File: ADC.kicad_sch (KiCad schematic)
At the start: 20 parts, among them U6 TLV320ADC5140IRTWR, U7 TLV320ADC5140IRTWR

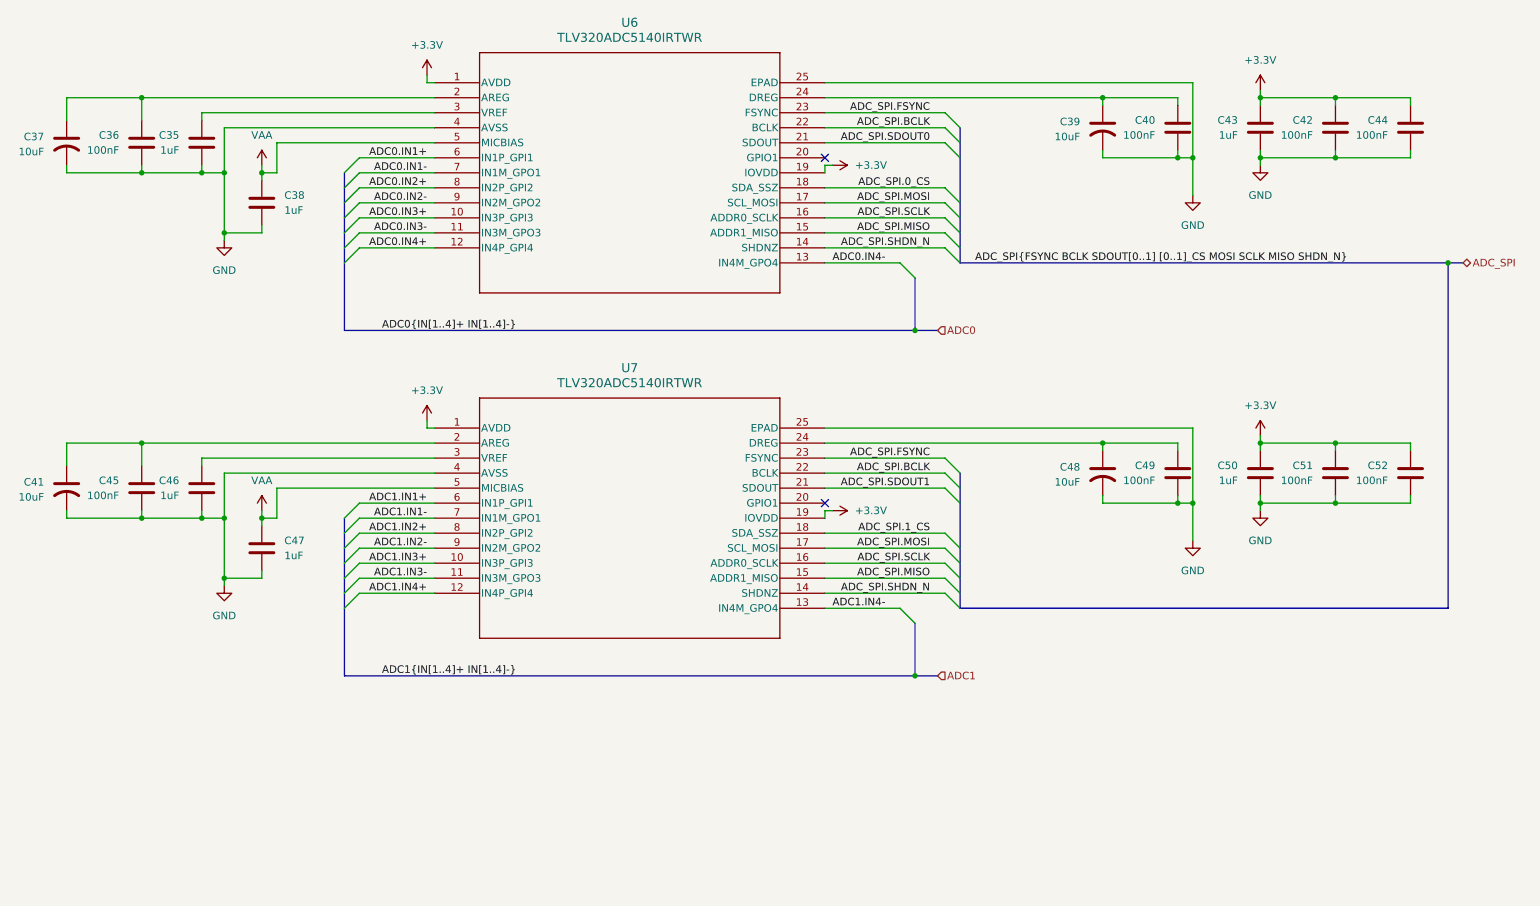
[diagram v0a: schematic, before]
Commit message: Added SRAM and removed old ADC
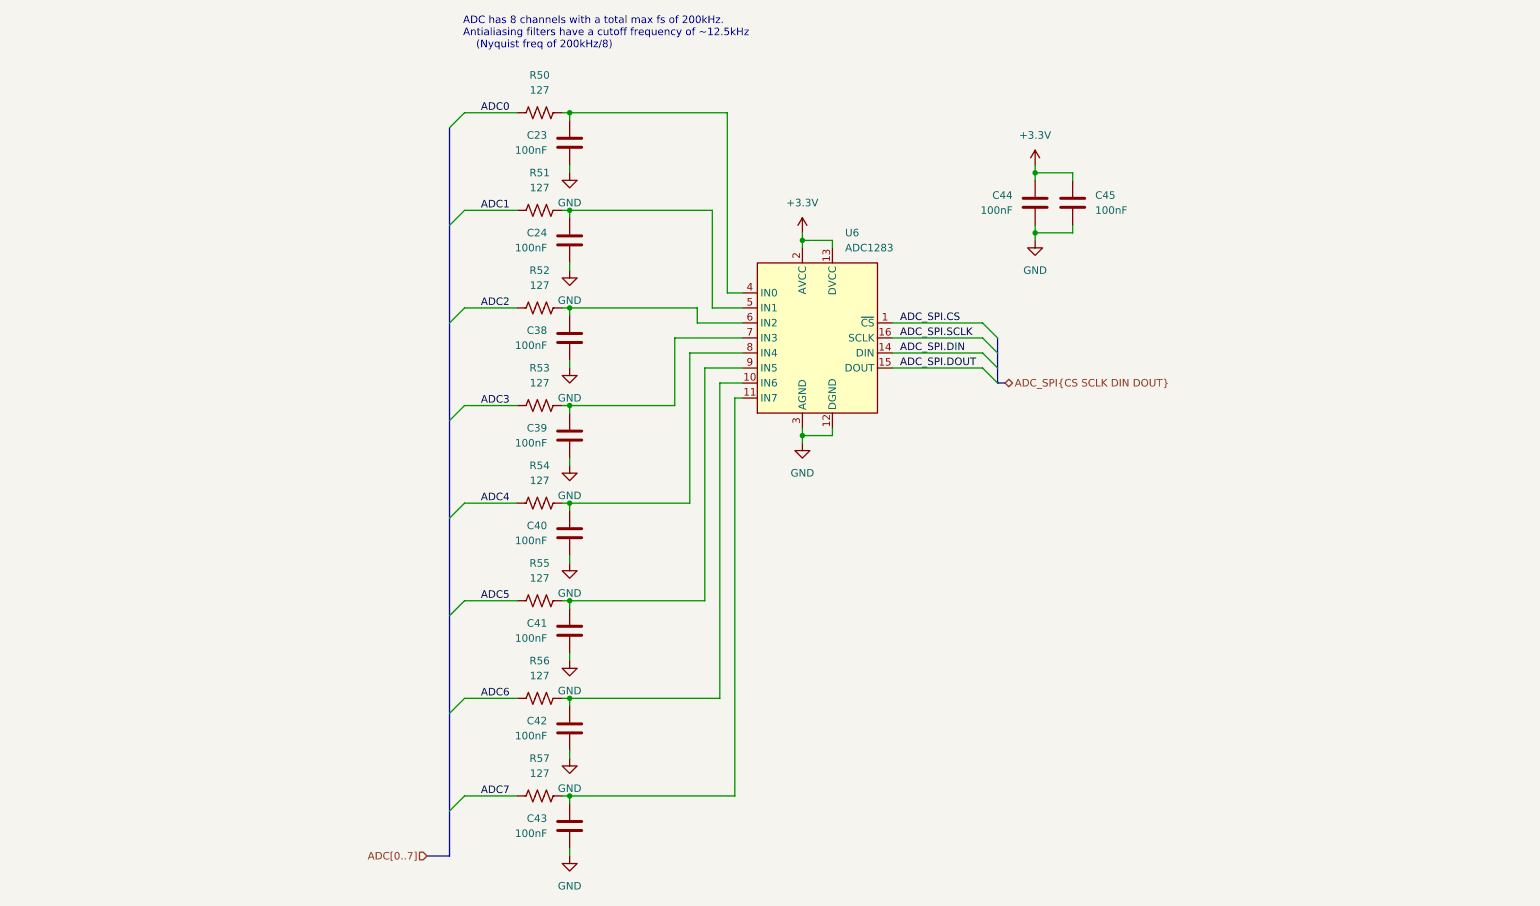
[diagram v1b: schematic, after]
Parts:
- removed C35, C46, C47, C50: 1uF, Capacitor_SMD:C_0603_1608Metric, symbol Device:C
- removed C36, C49, C51, C52: 100nF, Capacitor_SMD:C_0603_1608Metric, symbol Device:C
- removed C37, C39, C41, C48: 10uF, symbol Device:C_US
- removed U6, U7: TLV320ADC5140IRTWR, TLV320ADC5140:RTW24_4P15X4P15_TEX, symbol TLV320ADC5140:TLV320ADC5140IRTWR
- added C23, C24, C39, C41: 100nF, Capacitor_SMD:C_0603_1608Metric, symbol Device:C
- added R50, R51, R52, R53, R54, R55, R56, R57: 127, Resistor_SMD:R_0603_1608Metric, symbol Device:R_US
- added U6: ADC1283, Package_SO:TSSOP-16_4.4x5mm_P0.65mm, symbol Analog_ADC:ADC1283
- C38, C43: value 1uF -> 100nF
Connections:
- net +3.3V: now also C45.1, U6.13 (DVCC), U6.2 (AVCC); no longer C42.1, C43.1
- net ADC0: now also R50.1
- net ADC1: now also R51.1
- net ADC_SPI.SCLK: now also U6.16 (SCLK)
- net GND: now also C23.2, C24.2, C39.2, C41.2, U6.12 (DGND), U6.3 (AGND)
- net at C40.1: now also R54.2, U6.8 (IN4)
- net VAA: no longer names the net of C38.1
- net VAA: now also R52.2, U6.6 (IN2)
- new net: C24.1, R51.2, U6.5 (IN1)
- new net: C23.1, R50.2, U6.4 (IN0)
- new net: C42.1, R56.2, U6.10 (IN6)
- new net: C41.1, R55.2, U6.9 (IN5)
- new net: C43.1, R57.2, U6.11 (IN7)
- new net: C39.1, R53.2, U6.7 (IN3)
- new net ADC2: R52.1
- new net ADC3: R53.1
- new net ADC4: R54.1
- new net ADC5: R55.1
- new net ADC6: R56.1
- new net ADC7: R57.1
- new net ADC_SPI.CS: U6.1 (~{CS})
- new net ADC_SPI.DIN: U6.14 (DIN)
- new net ADC_SPI.DOUT: U6.15 (DOUT)
- no-connect marks 2 -> 0
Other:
- note added: "ADC has 8 channels with a total max fs of 200kHz. Antialiasing filters have a cutoff frequency of ~12.5kHz (Nyquist freq of 200kHz/8)"

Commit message: Initial design
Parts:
- C23, C24, C38, C39, C40, C41, C42, C43, C44, C45: Digikey PN (none) -> 1276-6854-1-ND; Unit Cost (none) -> 0.055
- R50, R51, R52, R53, R54, R55, R56, R57: Digikey PN (none) -> 311-127HRCT-ND; Unit Cost (none) -> 0.10
- U6: Digikey PN (none) -> 497-ADC1283IPTCT-ND; Unit Cost (none) -> 2.50

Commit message: Cleanup
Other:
- note added: "ADC has 8 channels with a total max fs of 200kHz. Antialiasing filters have a cutoff frequency of ~12.5kHz (200kHz/8/2)"
- note removed: "ADC has 8 channels with a total max fs of 200kHz. Antialiasing filters have a cutoff frequency of ~12.5kHz (Nyquist freq of 200kHz/8)"
- title: (none) -> ADC
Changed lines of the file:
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@@
 	(generator_version "10.0")
 	(paper "A4")
-	(text "ADC has 8 channels with a total max fs of 200kHz.\nAntialiasing filters have a cutoff frequency of ~12.5kHz \n	(Nyquist freq of 200kHz/8)"
+	(title_block
+		(title "ADC")
+		(date "2026-09-19")
+	)
+	(text "ADC has 8 channels with a total max fs of 200kHz.\nAntialiasing filters have a cutoff frequency of ~12.5kHz \n	(200kHz/8/2)"
 		(exclude_from_sim no)
 		(at 91.186 38.608 0)

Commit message: Annotated schematic
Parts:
- renumbered C23 to C56, C24 to C57, C38 to C58, C39 to C59, C40 to C60, C41 to C61, C42 to C62, C43 to C63, C44 to C64, C45 to C65, R50 to R65, R51 to R66, R52 to R67, R53 to R68, R54 to R69, R55 to R70, R56 to R71, R57 to R72, U6 to U8

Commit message: Started module-level layout
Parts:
- renumbered C56 to C57, C57 to C58, C58 to C59, C59 to C60, C60 to C61, C61 to C62, C62 to C63, C63 to C64, C64 to C65, C65 to C66, R65 to R67, R66 to R68, R67 to R69, R68 to R70, R69 to R71, R70 to R72, R71 to R73, R72 to R74, U8 to U9

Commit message: Added decal and gerbers
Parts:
- U9: Digikey PN 497-ADC1283IPTCT-ND -> ADC088S022CIMTX/NOPBCT-ND; Unit Cost 2.50 -> 3.52
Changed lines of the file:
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@@
 			)
 		)
-		(property "Digikey PN" "497-ADC1283IPTCT-ND"
+		(property "Digikey PN" "ADC088S022CIMTX/NOPBCT-ND"
 			(at 151.13 90.17 0)
 			(hide yes)
@@
 			)
 		)
-		(property "Unit Cost" "2.50"
+		(property "Unit Cost" "3.52"
 			(at 151.13 90.17 0)
 			(hide yes)
